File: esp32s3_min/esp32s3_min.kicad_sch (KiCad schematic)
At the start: 34 parts, among them U1 ESP32-S3, U2 PSRAM, U3 W25Q16JVSS, Y1 40MHz

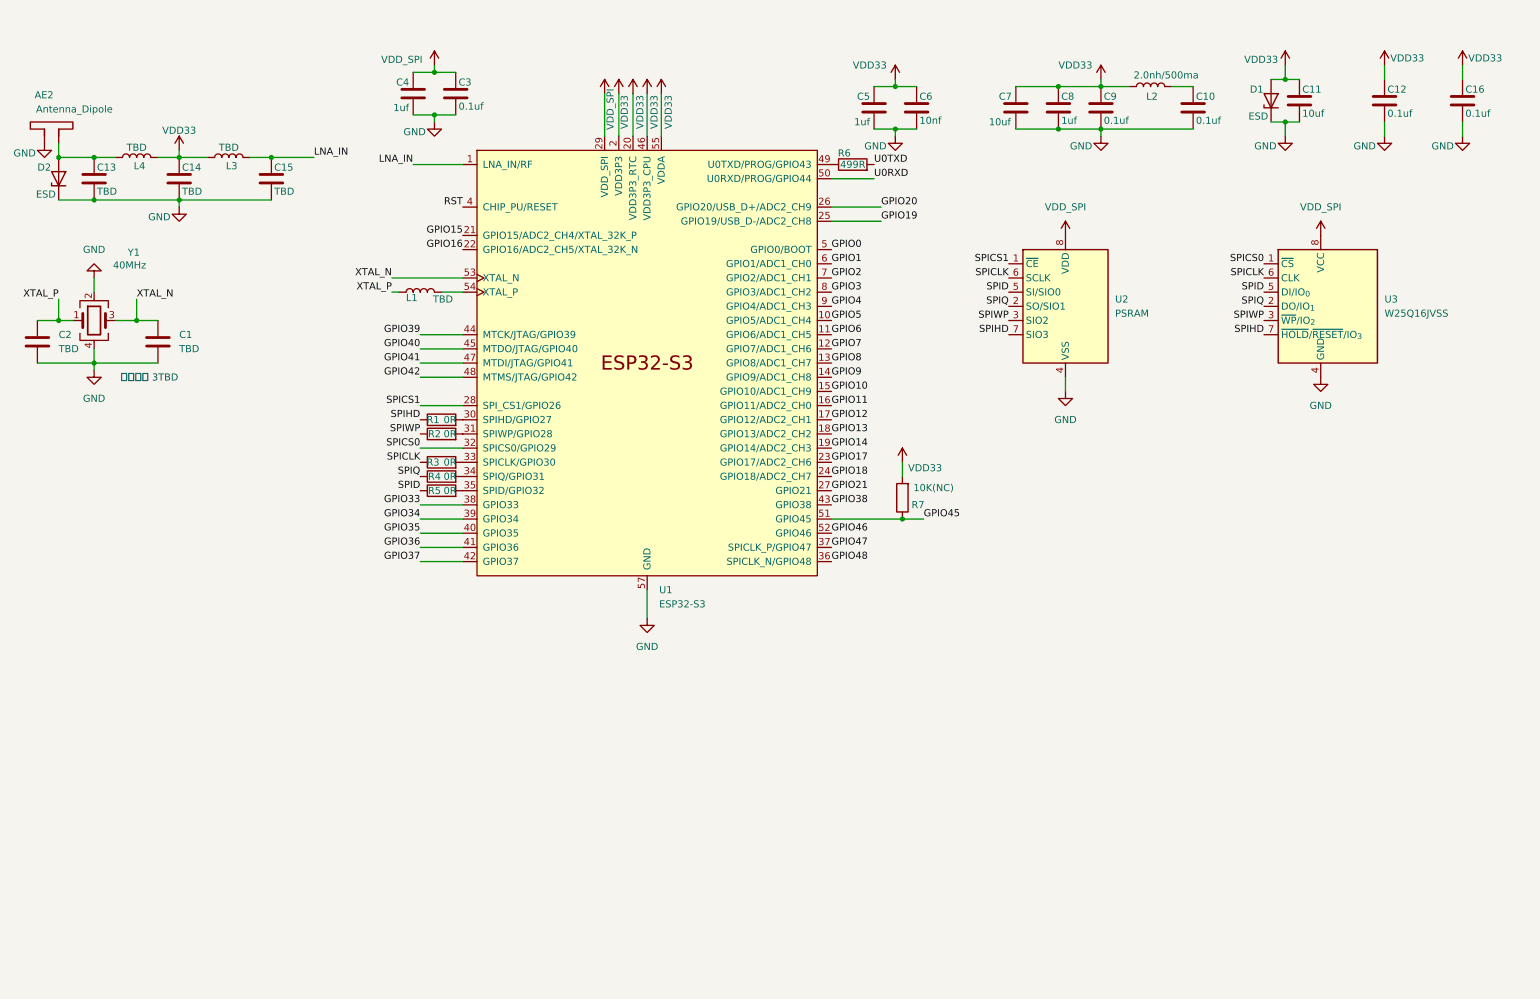
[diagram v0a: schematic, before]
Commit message: 引出引脚和usb接口的最小板
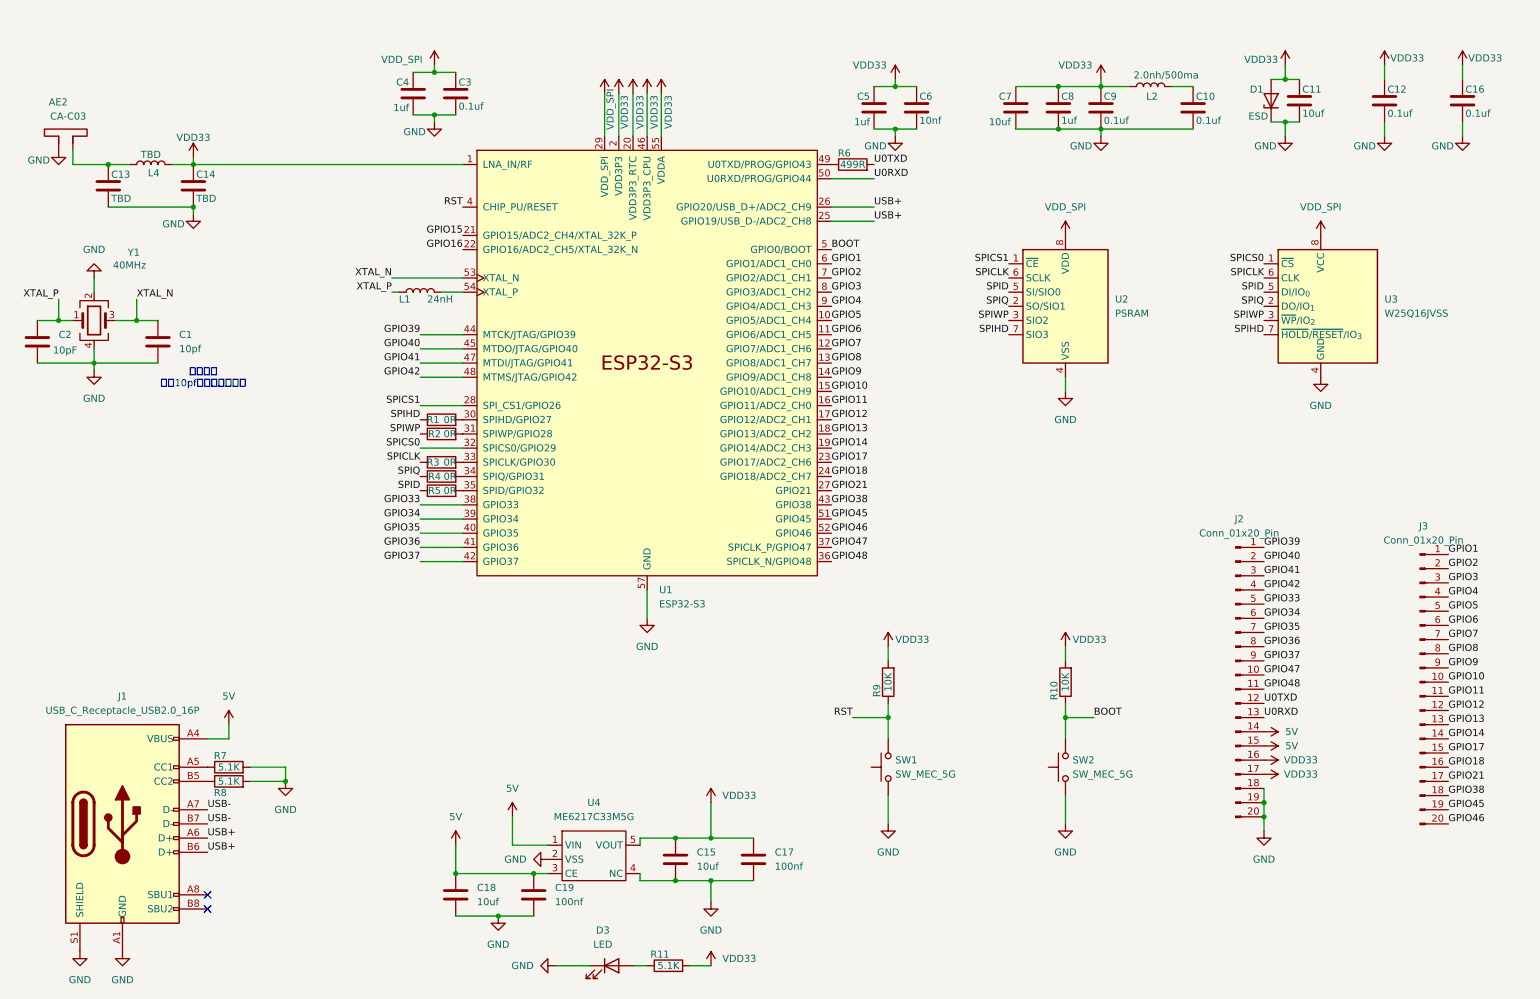
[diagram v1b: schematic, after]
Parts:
- removed D2: ESD, Diode_SMD:D_SOD-523, symbol Diode:ESD5Zxx
- removed L3: TBD, Inductor_SMD:L_0402_1005Metric, symbol Device:L
- added C17, C19: 100nf, Capacitor_SMD:C_0402_1005Metric, symbol Device:C
- added C18: 10uf, Capacitor_SMD:C_0402_1005Metric, symbol Device:C
- added D3: LED, LED_SMD:LED_0402_1005Metric, symbol Device:LED
- added J1: USB_C_Receptacle_USB2.0_16P, Connector_USB:USB_C_Receptacle_G-Switch_GT-USB-7010ASV, symbol Connector:USB_C_Receptacle_USB2.0_16P
- added J2, J3: Conn_01x20_Pin, Connector_PinHeader_1.00mm:PinHeader_1x20_P1.00mm_Vertical, symbol Connector:Conn_01x20_Pin
- added R10, R9: 10K, Resistor_SMD:R_0402_1005Metric, symbol Device:R
- added R11, R8: 5.1K, Resistor_SMD:R_0402_1005Metric, symbol Device:R
- added SW1, SW2: SW_MEC_5G, Button_Switch_SMD:SW_MEC_5GSH9, symbol Switch:SW_MEC_5G
- added U4: ME6217C33M5G, Package_TO_SOT_SMD:SOT-23-5, symbol myself:ME6217C33M5G
- AE2: value Antenna_Dipole -> CA-C03
- C1: value TBD -> 10pf
- C15: value TBD -> 10uf
- C2: value TBD -> 10pF
- L1: value TBD -> 24nH
- R7: value 10K(NC) -> 5.1K
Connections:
- net GPIO20 is gone; now on net USB+: U1.26 (GPIO20/USB_D+/ADC2_CH9)
- net LNA_IN is gone; now on net VDD33: C15.1, U1.1 (LNA_IN/RF)
- net GND: now also R7.2, C17.2, C18.2, C19.2, D3.1 (K), J1.A1 (GND), J1.A12 (GND), J1.B1 (GND), J1.B12 (GND), J1.S1 (SHIELD), J2.18 (Pin_18), J2.19 (Pin_19), J2.20 (Pin_20), R8.2, SW1.1 (A), SW1.2 (A), SW2.1 (A), SW2.2 (A), U4.2 (VSS), U4.4 (NC)
- net GPIO1: now also J3.1 (Pin_1)
- net GPIO10: now also J3.10 (Pin_10)
- net GPIO11: now also J3.11 (Pin_11)
- net GPIO12: now also J3.12 (Pin_12)
- net GPIO13: now also J3.13 (Pin_13)
- net GPIO14: now also J3.14 (Pin_14)
- net GPIO17: now also J3.15 (Pin_15)
- net GPIO18: now also J3.16 (Pin_16)
- net GPIO2: now also J3.2 (Pin_2)
- net GPIO21: now also J3.17 (Pin_17)
- net GPIO3: now also J3.3 (Pin_3)
- net GPIO33: now also J2.5 (Pin_5)
- net GPIO34: now also J2.6 (Pin_6)
- net GPIO35: now also J2.7 (Pin_7)
- net GPIO36: now also J2.8 (Pin_8)
- net GPIO37: now also J2.9 (Pin_9)
- net GPIO38: now also J3.18 (Pin_18)
- net GPIO39: now also J2.1 (Pin_1)
- net GPIO4: now also J3.4 (Pin_4)
- net GPIO40: now also J2.2 (Pin_2)
- net GPIO41: now also J2.3 (Pin_3)
- net GPIO42: now also J2.4 (Pin_4)
- net GPIO45: now also J3.19 (Pin_19); no longer R7.1
- net GPIO46: now also J3.20 (Pin_20)
- net GPIO47: now also J2.10 (Pin_10)
- net GPIO48: now also J2.11 (Pin_11)
- net GPIO5: now also J3.5 (Pin_5)
- net GPIO6: now also J3.6 (Pin_6)
- net GPIO7: now also J3.7 (Pin_7)
- net GPIO8: now also J3.8 (Pin_8)
- net GPIO9: now also J3.9 (Pin_9)
- net RST: now also R9.1, SW1.3 (B), SW1.4 (B)
- net U0RXD: now also J2.13 (Pin_13)
- net U0TXD: now also J2.12 (Pin_12)
- net VDD33: now also C17.1, J2.16 (Pin_16), J2.17 (Pin_17), R10.2, R11.2, R9.2, U4.5 (VOUT); no longer R7.2
- net GPIO0 renamed BOOT
- net BOOT: now also R10.1, SW2.3 (B), SW2.4 (B)
- net GPIO19 renamed USB+
- net USB+: now also J1.A6 (D+), J1.B6 (D+)
- new net: D3.2 (A), R11.1
- new net: J1.A5 (CC1), R7.1
- new net: J1.B5 (CC2), R8.1
- new net 5V: C18.1, C19.1, J1.A4 (VBUS), J1.A9 (VBUS), J1.B4 (VBUS), J1.B9 (VBUS), J2.14 (Pin_14), J2.15 (Pin_15), U4.1 (VIN), U4.3 (CE)
- new net USB-: J1.A7 (D-), J1.B7 (D-)
- no-connect marks 0 -> 2
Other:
- note added: "晶振电路 选择10pf匹配电容的晶振"
- note removed: "晶振电路 3TBD"
- moved on the sheet: AE2, C13, C14, L4

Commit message: 修改usb引脚，布局外围电路
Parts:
- removed C13, C14: TBD, Capacitor_SMD:C_0402_1005Metric, symbol Device:C
- removed L4: TBD, Inductor_SMD:L_0402_1005Metric, symbol Device:L
- removed SW1, SW2: SW_MEC_5G, Button_Switch_SMD:SW_MEC_5GSH9, symbol Switch:SW_MEC_5G
- removed U2: PSRAM, Package_SO:SOIC-8_3.9x4.9mm_P1.27mm, symbol Memory_RAM:APS1604M-3SQRx-SN
- added L3: 3nh, Inductor_SMD:L_0402_1005Metric, symbol Device:L
- added R12, R13: 0R, Resistor_SMD:R_0402_1005Metric, symbol Device:R
- added SW1, SW3: ~, myself:SW-SMD_L3.9-W3.6-LS4.8-EH, symbol myself:my_smd_key
- AE2: footprint (none) -> myself:CA-C03
- J2, J3: footprint Connector_PinHeader_1.00mm:PinHeader_1x20_P1.00mm_Vertical -> Connector_PinHeader_1.27mm:PinHeader_1x20_P1.27mm_Vertical
- Y1: footprint Crystal:Crystal_SMD_3225-4Pin_3.2x2.5mm_HandSoldering -> Crystal:Crystal_SMD_3225-4Pin_3.2x2.5mm
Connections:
- net BOOT: now also SW1.2
- net GND: now also L3.1, SW1.1, SW3.1
- net RST: now also SW3.2
- net USB+: no longer U1.25 (GPIO19/USB_D-/ADC2_CH8)
- net USB-: now also U1.25 (GPIO19/USB_D-/ADC2_CH8)
- net VDD33: no longer U1.1 (LNA_IN/RF)
- net at AE2.2: now also R13.1
- net SPICS1: no longer names the net of U1.28 (SPI_CS1/GPIO26)
- new net: L3.2, R12.1, R13.2
- new net: R12.2, U1.1 (LNA_IN/RF)
- no-connect marks 2 -> 3
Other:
- note added: "VDD3P3"
- note added: "VDD3P3_CPU"
- note added: "VDD3P3_RTC"
- note added: "VDDA"
- note added: "使用内置psram"
- moved on the sheet: U3
